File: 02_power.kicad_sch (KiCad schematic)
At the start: 22 parts, among them J5 UJ20-C-H-G-SMT-TR, J6 Conn_01x02_Socket, Q2 DMG2305UX-7, U2 BQ24090DGQ

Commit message: selfcontainment, smaller fixes
Signed-off-by: Anna-Lena Marx <anna-lena.marx@web.de>
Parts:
- S2: footprint 4504040015514:450404015514 -> prj-footprints:450404015514
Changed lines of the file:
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@@
 			)
 		)
-		(property "Footprint" "4504040015514:450404015514"
+		(property "Footprint" "prj-footprints:450404015514"
 			(at 238.76 64.77 0)
 			(effects
@@
 		(pin "1"
 		)
+		(pin "2"
+		)
 		(pin "3"
 		)
-		(pin "2"
-		)
 		(instances
-			(project "ZEReader-Pico"
+			(project ""
 				(path "/ec954637-2a8b-4662-b4a1-f88107f11cb0/a18230d5-251f-4044-a9cd-045093d87cd6"
 					(reference "S2")

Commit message: selfcontainment fixes
Signed-off-by: Anna-Lena Marx <anna-lena.marx@web.de>
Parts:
- S2: Description_1 Slide Switch SPDT Surface Mount -> Slide Switch SPDT Surface Mount
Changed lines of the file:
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@@
 			)
 		)
-		(property "Datasheet" ""
+		(property "Datasheet" "https://www.diodes.com/assets/Datasheets/DMG2305UX.pdf"
 			(at 204.47 64.77 0)
 			(effects
@@
 			)
 		)
-		(property "Datasheet" ""
+		(property "Datasheet" "https://www.we-online.com/components/products/datasheet/450404015514.pdf"
 			(at 238.76 64.77 0)
 			(effects
@@
 			)
 		)
-		(property "Description_1" "\n                        \n                            Slide Switch SPDT Surface Mount\n                        \n"
+		(property "Description_1" "Slide Switch SPDT Surface Mount"
 			(at 238.76 64.77 0)
 			(effects
@@
 			)
 		)
-		(property "Datasheet" ""
+		(property "Datasheet" "https://www.sameskydevices.com/product/resource/uj20-c-h-g-smt-tr.pdf"
 			(at 25.4 76.2 0)
 			(effects

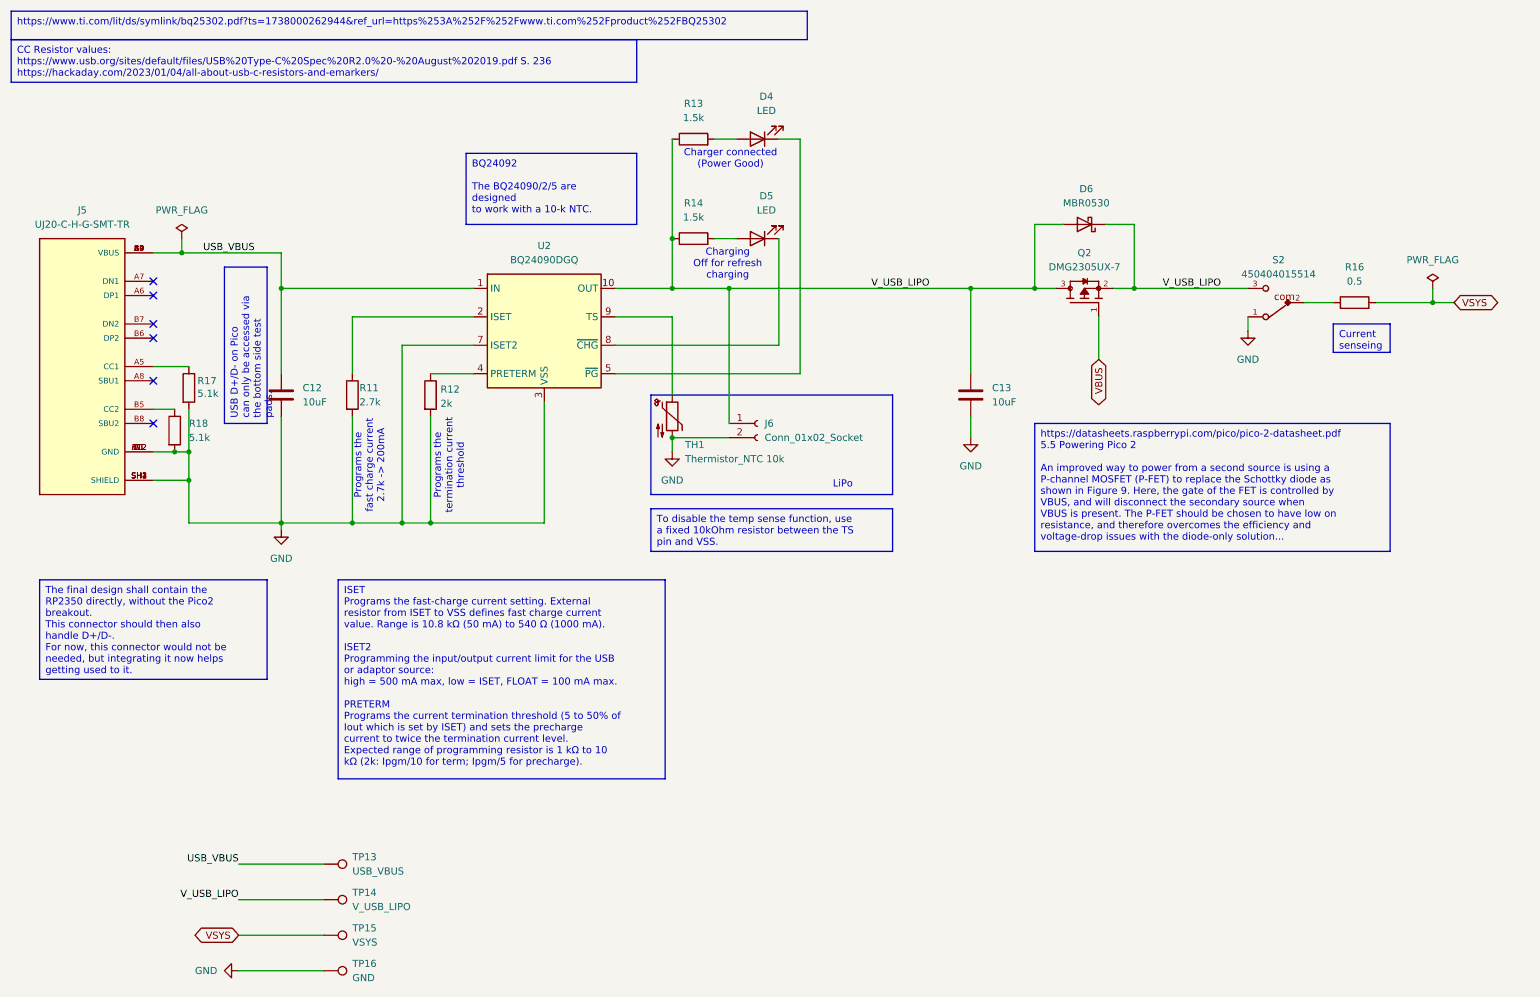
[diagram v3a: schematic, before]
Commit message: Imported Aisler design rules, routed power and display booster
Signed-off-by: Anna-Lena Marx <anna-lena.marx@web.de>
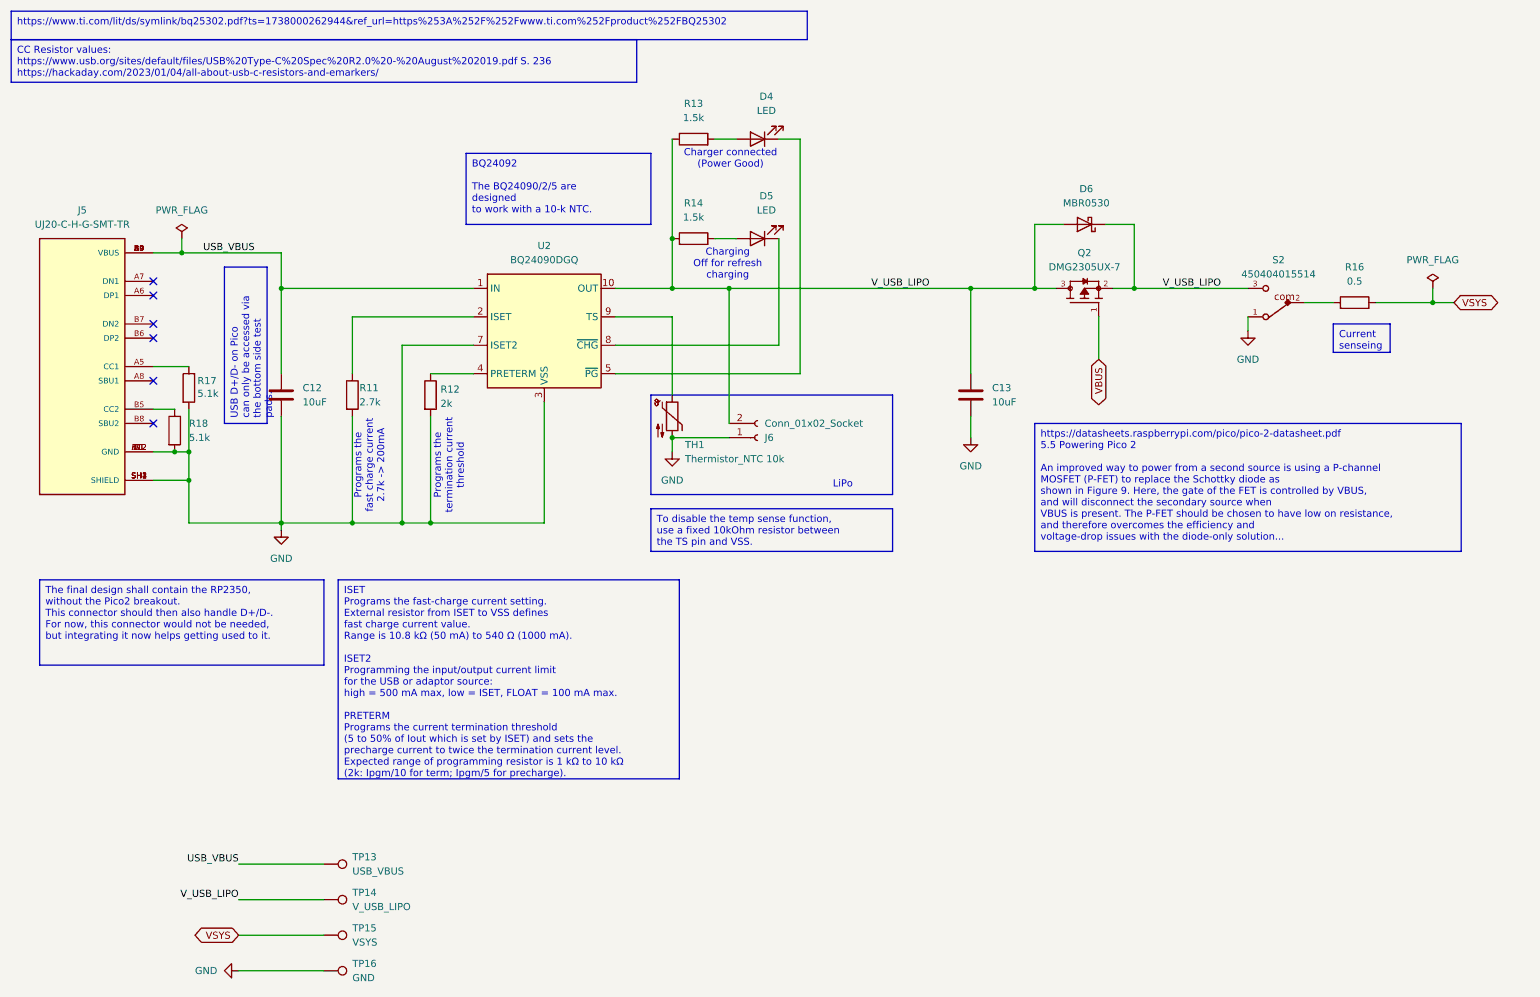
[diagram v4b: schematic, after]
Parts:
- J5: Description_1 Type C, USB 2.0, 480 Mbps, 20 Vdc, 5 A, Right Angle, Gold Flash, Surface Mount, Black Insulator, USB Receptacle -> Type C, USB 2.0, 480 Mbps, 20 Vdc, 5 A, Right Angle, Gold Flash, Surface Mount, Black Insulator, USB Receptacle
- Q2: Description_1 MOSFET P-Ch 20V 5A Enhancement SOT23 | Diodes Inc DMG2305UX-7 -> MOSFET P-Ch 20V 5A Enhancement SOT23 | Diodes Inc DMG2305UX-7
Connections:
- net GND: now also J6.1 (Pin_1); no longer J6.2 (Pin_2)
- net V_USB_LIPO: now also J6.2 (Pin_2); no longer J6.1 (Pin_1)
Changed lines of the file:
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@@
 		)
 	)
-	(text_box "To disable the temp sense function, use a fixed 10kOhm resistor between the TS pin and VSS."
+	(text_box "To disable the temp sense function, \nuse a fixed 10kOhm resistor between \nthe TS pin and VSS."
 		(exclude_from_sim no)
 		(at 127 101.6 0)
@@
 		(exclude_from_sim no)
 		(at 93.98 38.1 0)
-		(size 30.48 12.7)
+		(size 33.02 12.7)
 		(stroke
 			(width 0)
@@
 		)
 	)
-	(text_box "https://datasheets.raspberrypi.com/pico/pico-2-datasheet.pdf\n5.5 Powering Pico 2\n\nAn improved way to power from a second source is using a P-channel MOSFET (P-FET) to replace the Schottky diode as\nshown in Figure 9. Here, the gate of the FET is controlled by VBUS, and will disconnect the secondary source when\nVBUS is present. The P-FET should be chosen to have low on resistance, and therefore overcomes the efficiency and\nvoltage-drop issues with the diode-only solution..."
+	(text_box "https://datasheets.raspberrypi.com/pico/pico-2-datasheet.pdf\n5.5 Powering Pico 2\n\nAn improved way to power from a second source is using a P-channel \nMOSFET (P-FET) to replace the Schottky diode as\nshown in Figure 9. Here, the gate of the FET is controlled by VBUS,\nand will disconnect the secondary source when\nVBUS is present. The P-FET should be chosen to have low on resistance,\nand therefore overcomes the efficiency and\nvoltage-drop issues with the diode-only solution..."
 		(exclude_from_sim no)
 		(at 195.58 86.36 0)
-		(size 63.5 22.86)
+		(size 76.2 22.86)
 		(stroke
 			(width 0)
@@
 		)
 	)
-	(text_box "ISET\nPrograms the fast-charge current setting. External resistor from ISET to VSS defines fast charge current\nvalue. Range is 10.8 kΩ (50 mA) to 540 Ω (1000 mA).\n\nISET2\nProgramming the input/output current limit for the USB or adaptor source:\nhigh = 500 mA max, low = ISET, FLOAT = 100 mA max.\n\nPRETERM\nPrograms the current termination threshold (5 to 50% of Iout which is set by ISET) and sets the precharge current to twice the termination current level.\nExpected range of programming resistor is 1 kΩ to 10 kΩ (2k: Ipgm/10 for term; Ipgm/5 for precharge)."
+	(text_box "ISET\nPrograms the fast-charge current setting.\nExternal resistor from ISET to VSS defines \nfast charge current value.\nRange is 10.8 kΩ (50 mA) to 540 Ω (1000 mA).\n\nISET2\nProgramming the input/output current limit \nfor the USB or adaptor source:\nhigh = 500 mA max, low = ISET, FLOAT = 100 mA max.\n\nPRETERM\nPrograms the current termination threshold \n(5 to 50% of Iout which is set by ISET) and sets the \nprecharge current to twice the termination current level.\nExpected range of programming resistor is 1 kΩ to 10 kΩ\n(2k: Ipgm/10 for term; Ipgm/5 for precharge)."
 		(exclude_from_sim no)
 		(at 71.12 114.3 0)
-		(size 58.42 35.56)
+		(size 60.96 35.56)
 		(stroke
 			(width 0)
@@
 		)
 	)
-	(text_box "The final design shall contain the RP2350 directly, without the Pico2 breakout.\nThis connector should then also handle D+/D-.\nFor now, this connector would not be needed, but integrating it now helps getting used to it."
+	(text_box "The final design shall contain the RP2350,\nwithout the Pico2 breakout.\nThis connector should then also handle D+/D-.\nFor now, this connector would not be needed, \nbut integrating it now helps getting used to it."
 		(exclude_from_sim no)
 		(at 17.78 114.3 0)
-		(size 40.64 17.78)
+		(size 50.8 15.24)
 		(stroke
 			(width 0)
@@
 		)
 	)
-	(text_box "Current senseing"
+	(text_box "Current\nsenseing"
 		(exclude_from_sim no)
 		(at 248.92 68.58 0)
@@
 		)
 	)
+	(netclass_flag ""
+		(length 2.54)
+		(shape round)
+		(at 160.02 62.23 0)
+		(fields_autoplaced yes)
+		(effects
+			(font
+				(size 1.27 1.27)
+			)
+			(justify left bottom)
+		)
+		(property "Netclass" "PWR"
+			(at 160.7185 59.69 0)
+			(effects
+				(font
+					(size 1.27 1.27)
+					(italic yes)
+				)
+				(justify left)
+			)
+		)
+	)
+	(netclass_flag ""
+		(length 2.54)
+		(shape round)
+		(at 53.34 104.14 0)
+		(fields_autoplaced yes)
+		(effects
+			(font
+				(size 1.27 1.27)
+			)
+			(justify left bottom)
+		)
+		(property "Netclass" "GND"
+			(at 54.0385 101.6 0)
+			(effects
+				(font
+					(size 1.27 1.27)
+					(italic yes)
+				)
+				(justify left)
+			)
+		)
+	)
+	(netclass_flag ""
+		(length 2.54)
+		(shape round)
+		(at 207.01 72.39 90)
+		(fields_autoplaced yes)
+		(effects
+			(font
+				(size 1.27 1.27)
+			)
+			(justify left bottom)
+		)
+		(property "Netclass" "PWR"
+			(at 204.47 71.6915 90)
+			(effects
+				(font
+					(size 1.27 1.27)
+					(italic yes)
+				)
+				(justify left)
+			)
+		)
+	)
+	(netclass_flag ""
+		(length 2.54)
+		(shape round)
+		(at 38.1 55.88 0)
+		(fields_autoplaced yes)
+		(effects
+			(font
+				(size 1.27 1.27)
+			)
+			(justify left bottom)
+		)
+		(property "Netclass" "PWR"
+			(at 38.7985 53.34 0)
+			(effects
+				(font
+					(size 1.27 1.27)
+					(italic yes)
+				)
+				(justify left)
+			)
+		)
+	)
+	(netclass_flag ""
+		(length 2.54)
+		(shape round)
+		(at 260.35 64.77 0)
+		(fields_autoplaced yes)
+		(effects
+			(font
+				(size 1.27 1.27)
+			)
+			(justify left bottom)
+		)
+		(property "Netclass" "PWR"
+			(at 261.0485 62.23 0)
+			(effects
+				(font
+					(size 1.27 1.27)
+					(italic yes)
+				)
+				(justify left)
+			)
+		)
+	)
 	(symbol
 		(lib_id "Connector:TestPoint")
@@
 	(symbol
 		(lib_id "Connector:Conn_01x02_Socket")
-		(at 146.05 86.36 0)
+		(at 146.05 88.9 0)
+		(mirror x)
 		(unit 1)
 		(exclude_from_sim no)
@@
 		(on_board yes)
 		(dnp no)
-		(fields_autoplaced yes)
 		(property "Reference" "J6"
-			(at 147.32 86.3599 0)
+			(at 147.32 88.9001 0)
 			(effects
 				(font
@@
 		)
 		(property "Value" "Conn_01x02_Socket"
-			(at 147.32 88.8999 0)
+			(at 147.32 86.3601 0)
 			(effects
 				(font
@@
 		)
 		(property "Footprint" "Connector_JST:JST_EH_S2B-EH_1x02_P2.50mm_Horizontal"
-			(at 146.05 86.36 0)
+			(at 146.05 88.9 0)
 			(effects
 				(font
@@
 		)
 		(property "Datasheet" "~"
-			(at 146.05 86.36 0)
+			(at 146.05 88.9 0)
 			(effects
 				(font
@@
 		)
 		(property "Description" "Generic connector, single row, 01x02, script generated"
-			(at 146.05 86.36 0)
+			(at 146.05 88.9 0)
 			(effects
 				(font
@@
 			)
 		)
-		(property "Description_1" "\n                        \n                            MOSFET P-Ch 20V 5A Enhancement SOT23 | Diodes Inc DMG2305UX-7\n                        \n"
+		(property "Description_1" "MOSFET P-Ch 20V 5A Enhancement SOT23 | Diodes Inc DMG2305UX-7                \n"
 			(at 204.47 64.77 0)
 			(effects
@@
 			)
 		)
-		(property "Description_1" "\n                        \n                            Type C, USB 2.0, 480 Mbps, 20 Vdc, 5 A, Right Angle, Gold Flash, Surface Mount, Black Insulator, USB Receptacle\n                        \n"
+		(property "Description_1" "Type C, USB 2.0, 480 Mbps, 20 Vdc, 5 A, Right Angle, Gold Flash, Surface Mount, Black Insulator, USB Receptacle"
 			(at 25.4 76.2 0)
 			(effects

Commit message: Changed USB connector due to manufacturing rule violations
Signed-off-by: Anna-Lena Marx <anna-lena.marx@web.de>
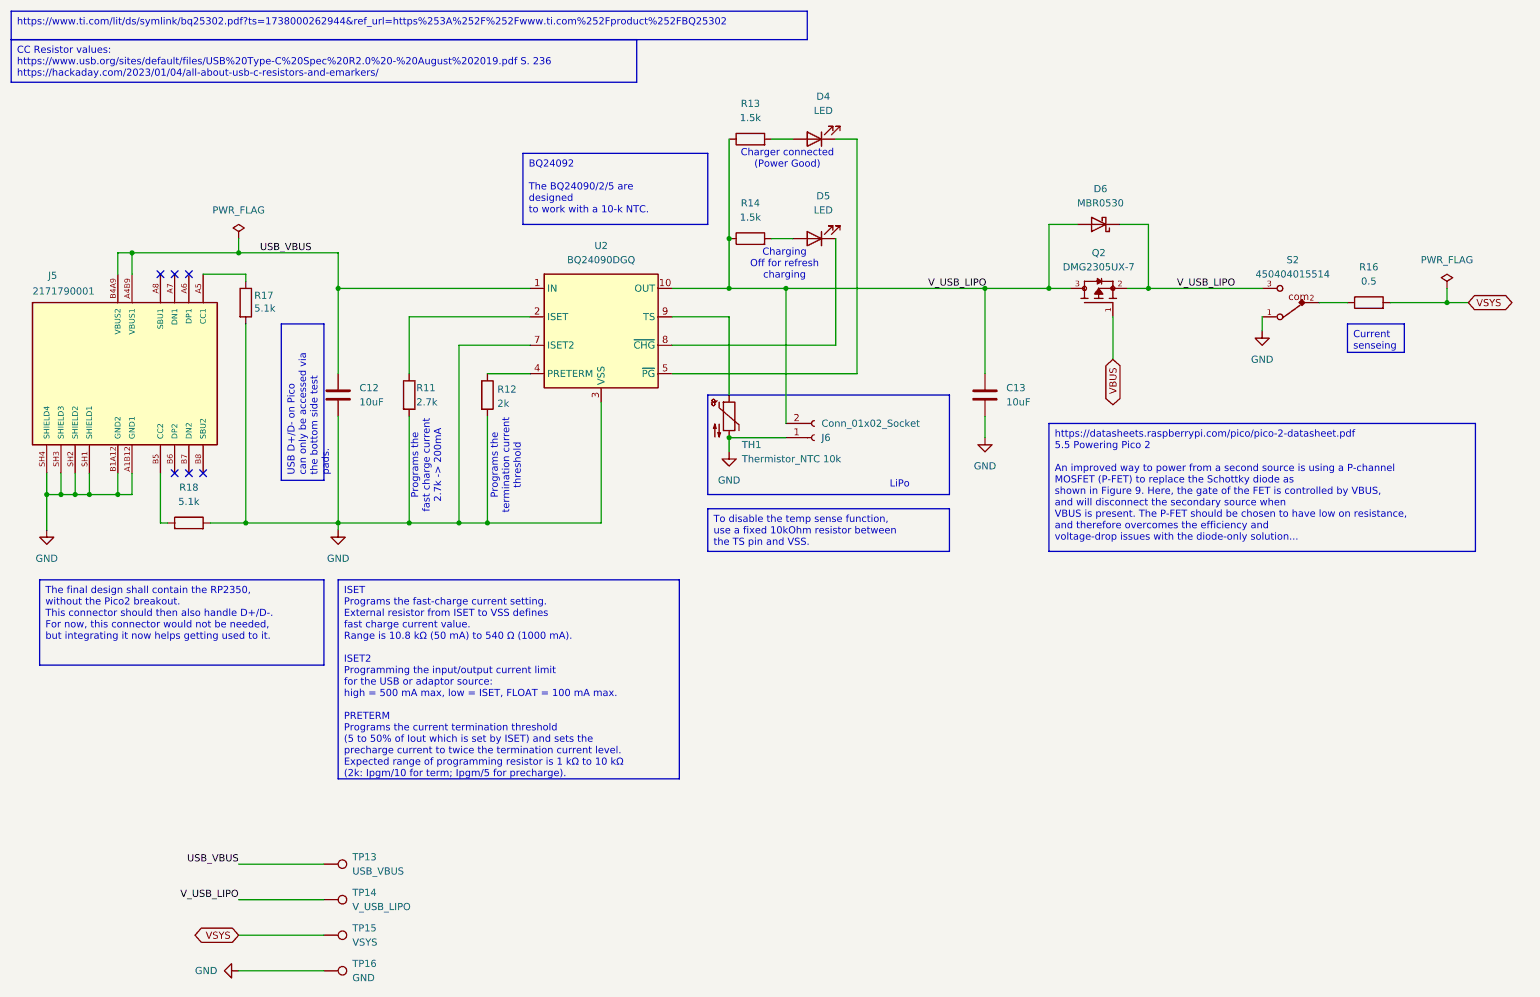
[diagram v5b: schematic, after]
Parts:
- removed J5: UJ20-C-H-G-SMT-TR, prj-footprints:CUI_UJ20-C-H-G-SMT-TR, symbol UJ20-C-H-G-SMT-TR:UJ20-C-H-G-SMT-TR
- added J5: 2171790001, prj-footprints:MOLEX_2171790001, symbol 2171790001:2171790001
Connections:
- net GND: now also J5.A1B12 (GND1), J5.B1A12 (GND2), J5.SH1 (SHIELD1), J5.SH2 (SHIELD2), J5.SH3 (SHIELD3), J5.SH4 (SHIELD4)
- net USB_VBUS: now also J5.A4B9 (VBUS1), J5.B4A9 (VBUS2)
- net at R18.1: now also J5.B5 (CC2)
- net at R17.1: now also J5.A5 (CC1)
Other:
- moved on the sheet: C12, C13, D4, D5, D6, J6, Q2, R11, R12, R13, R14, R16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
